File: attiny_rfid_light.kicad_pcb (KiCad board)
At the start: 2 copper layers, 76 x 99.1 mm, 27 parts, among them IC1 EM4095, U1 ESP32-WROOM-32, U2 NCP1117-3.3_SOT223

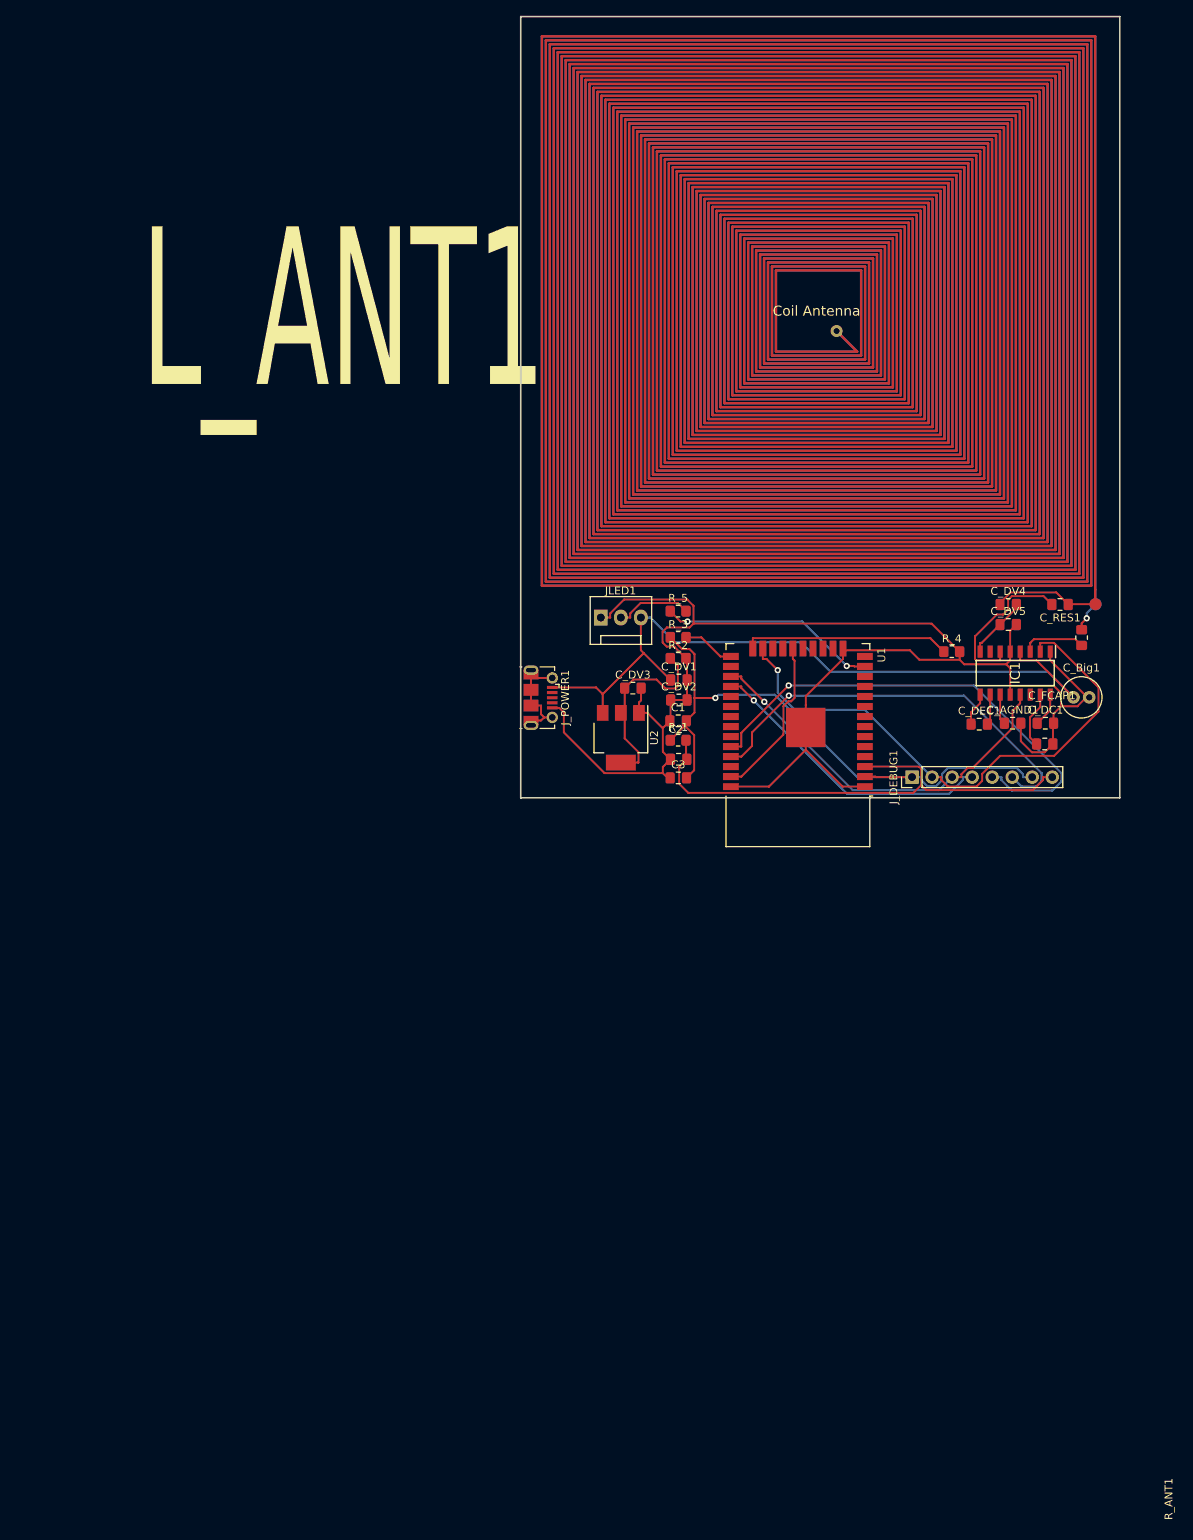
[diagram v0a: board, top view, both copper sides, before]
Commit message: Update fix antenna direction and missing shd trace
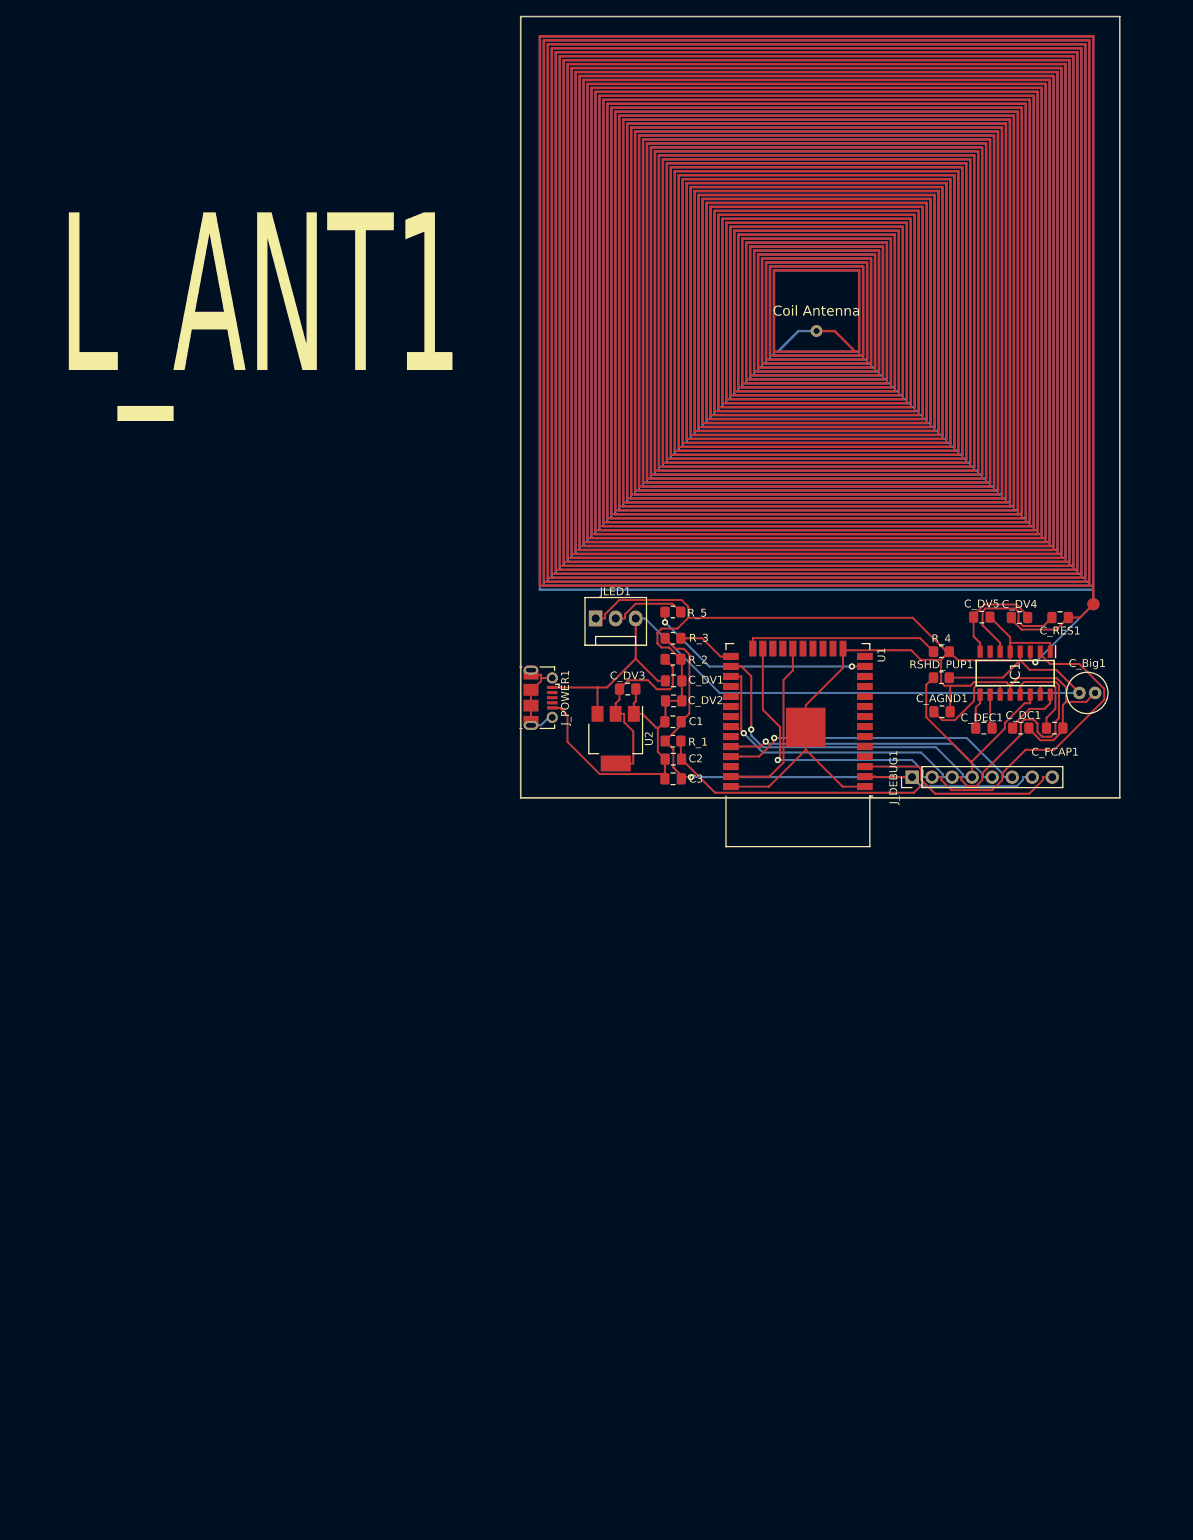
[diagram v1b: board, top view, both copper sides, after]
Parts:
- removed R_ANT1: 10, Resistor_SMD:R_0805_2012Metric_Pad1.20x1.40mm_HandSolder
- added RSHD_PUP1: 10K, Resistor_SMD:R_0805_2012Metric_Pad1.20x1.40mm_HandSolder, F.Cu at (119.4, 139.7)
- C_AGND1, C_DEC1: value C -> 100nf
- C_DC1: value C -> 10NF
- C_DV4: value C -> 0.1nf
- C_DV5: value C -> 3.7nf
- C_FCAP1: value C -> 10nf
- C_RES1: value C -> 2.2nf
- L_ANT1: footprint pcb_inductors:60_turn_square_inductor -> pcb_inductors:60_turn_square_inductor_corrected
- moved C_AGND1 9.07 mm to (119.5, 144.0)
- moved C_DV5 3.47 mm to (124.5, 132.0)
- moved C_DC1 3.18 mm to (129.4, 146.1)
- moved C_FCAP1 2.38 mm to (133.7, 146.1)
- moved C_DV4 2.19 mm to (129.3, 132.1)
- moved C_RES1 1.65 mm to (134.4, 132.1)
- moved R_4 1.32 mm to (119.4, 136.4)
- moved C_Big1 0.94 mm to (136.9, 141.6)
- moved C_DEC1 0.78 mm to (124.8, 146.1)
- moved C2 0.67 mm to (85.4, 150.0)
- moved C1 0.67 mm to (85.3, 145.3)
- moved C_DV1 0.67 mm to (85.4, 140.1)
- moved C_DV2 0.67 mm to (85.4, 142.6)
- moved R_3 0.67 mm to (85.4, 134.7)
- moved R_5 0.67 mm to (85.3, 131.4)
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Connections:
- IC1 pad 14: unconnected-(IC1-Pad14) -> Net-(IC1-Pad14)
- J_DEBUG1 pad 4: Net-(J_DEBUG1-Pad4) -> Net-(IC1-Pad14)
- L_ANT1 pad 2: Net-(L_ANT1-Pad2) -> Net-(IC1-Pad3)
- U1 pad 26: unconnected-(U1-Pad26) -> Net-(IC1-Pad14)
- U1 pad 28: Net-(J_DEBUG1-Pad4) -> unconnected-(U1-Pad28)
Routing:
- net Net-(IC1-Pad14): track 0.00 -> 68.5 mm, vias 0 -> 1
- net Net-(J_DEBUG1-Pad4): track 37.4 -> 0.00 mm, vias 1 -> 0
- net Net-(J_DEBUG1-Pad5): track 62.0 -> 35.5 mm
- net Net-(IC1-Pad13): track 50.0 -> 70.6 mm
- net Net-(J_DEBUG1-Pad6): track 53.2 -> 39.2 mm
- net +5V: track 94.8 -> 105.9 mm
- net GND: track 205.9 -> 215.1 mm
- net Net-(C_AGND1-Pad1): track 3.85 -> 12.7 mm
- net +3V3: track 79.8 -> 73.5 mm
- net Net-(C_DV4-Pad2): track 7.98 -> 13.2 mm
- net Net-(IC1-Pad2): track 70.8 -> 75.7 mm
- net Net-(IC1-Pad3): track 8.15 -> 12.3 mm, vias 0 -> 1
- net Net-(L_ANT1-Pad2): track 3.96 -> 0.00 mm, vias 1 -> 0
- net Net-(C_RES1-Pad2): track 20.3 -> 17.1 mm
- net Net-(C_DC1-Pad1): track 4.32 -> 7.36 mm
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
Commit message: v3
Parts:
- removed C3: 1uf, Capacitor_SMD:C_0805_2012Metric_Pad1.18x1.45mm_HandSolder
- removed R_5: 490, Resistor_SMD:R_0805_2012Metric_Pad1.20x1.40mm_HandSolder
- added C_RESOptional1: NA, Capacitor_SMD:C_0805_2012Metric_Pad1.18x1.45mm_HandSolder, F.Cu at (131.9, 130.6)
- added m2: MountingHole_2.1mm, MountingHole:MountingHole_2.1mm, F.Cu at (114.3, 132.1)
- added m2: MountingHole_2.1mm, MountingHole:MountingHole_2.1mm, F.Cu at (68.6, 132.1)
- added m2: MountingHole_2.1mm, MountingHole:MountingHole_2.1mm, F.Cu at (138.4, 152.6)
- added m2: MountingHole_2.1mm, MountingHole:MountingHole_2.1mm, F.Cu at (68.4, 152.4)
- C1: value 100uf -> 0.1uf
- C2: value 0.1uf -> 1uf
- C_Big1: value 10uf -> 100uf
- C_DV3: value 22uf -> 0.1nf
- C_DV4: value 0.1nf -> 3.7nf split between 2
- C_DV5: value 3.7nf -> 3.7nf split between 2
- R_2: value 3.3k -> 5k1 or 5k? was 5k og
- R_3: value 5k -> 490
- R_4: value 5k -> 5k1 og was 5k
- moved C1 51.4 mm to (136.6, 149.2), turned to 180 degrees
- moved C_DV3 42.6 mm to (121.5, 133.1)
- moved C_DV1 40.4 mm to (125.4, 146.3)
- moved C2 32.6 mm to (115.8, 138.5)
- moved R_4 32.0 mm to (87.4, 137.2)
- moved R_1 30.8 mm to (115.8, 143.3), turned to 180 degrees
- moved C_AGND1 11.9 mm to (131.1, 146.3)
- moved C_DV2 10.1 mm to (87.5, 152.5)
- moved RSHD_PUP1 8.53 mm to (116.0, 147.5)
- moved C_DC1 7.19 mm to (136.6, 145.8)
- moved C_DEC1 5.18 mm to (121.0, 142.6), turned to 90 degrees
- moved C_FCAP1 4.82 mm to (136.6, 142.2)
- moved C_Big1 4.48 mm to (136.9, 137.2)
- moved C_DV4 3.32 mm to (126.4, 130.5)
- moved R_2 3.17 mm to (87.5, 139.7)
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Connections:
- C1 pad 2: +3V3 -> Net-(C1-Pad2)
- C2 pad 2: Net-(C2-Pad2) -> +3V3
- C_DV2 pad 1: GND -> +3V3
- C_DV3 pad 2: GND -> Net-(C_DV3-Pad2)
- C_DV4 pad 1: Net-(C_DV4-Pad1) -> Net-(C_DV3-Pad2)
- C_DV4 pad 2: Net-(C_DV4-Pad2) -> GND
- C_DV5 pad 1: Net-(C_DV4-Pad2) -> Net-(C_DV3-Pad2)
- C_RES1 pad 1: Net-(C_DV4-Pad1) -> Net-(C_DV3-Pad1)
- IC1 pad 7: unconnected-(IC1-Pad7) -> +5V
- IC1 pad 8: Net-(C_DV4-Pad2) -> Net-(C_DV3-Pad2)
- J_DEBUG1 pad 1: +3V3 -> GND
- J_DEBUG1 pad 2: Net-(IC1-Pad2) -> +3V3
- J_DEBUG1 pad 3: Net-(IC1-Pad13) -> +5V
- J_DEBUG1 pad 4: Net-(IC1-Pad14) -> Net-(J_DEBUG1-Pad4)
- J_DEBUG1 pad 7: +3V3 -> Net-(J_DEBUG1-Pad7)
- J_DEBUG1 pad 8: Net-(C2-Pad2) -> Net-(C1-Pad2)
- L_ANT1 pad 1: Net-(C_DV4-Pad1) -> Net-(C_DV3-Pad1)
- R_1 pad 2: Net-(C2-Pad2) -> Net-(C1-Pad2)
- R_2 pad 1: Net-(C_DV3-Pad1) -> +3V3
- R_2 pad 2: GND -> Net-(J_DEBUG1-Pad7)
- R_3 pad 1: +3V3 -> Net-(JLED1-Pad2)
- U1 pad 13: Net-(R_5-Pad1) -> Net-(R_3-Pad2)
- U1 pad 25: Net-(R_3-Pad2) -> Net-(J_DEBUG1-Pad7)
- U1 pad 29: unconnected-(U1-Pad29) -> Net-(J_DEBUG1-Pad4)
- U1 pad 3: Net-(C2-Pad2) -> Net-(C1-Pad2)
- U2 pad 2: Net-(C_DV3-Pad1) -> +3V3
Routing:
- net Net-(C2-Pad2): track 62.4 -> 0.00 mm
- net Net-(J_DEBUG1-Pad7): track 0.00 -> 50.1 mm, vias 0 -> 1
- net Net-(J_DEBUG1-Pad4): track 0.00 -> 37.8 mm, vias 0 -> 1
- net Net-(IC1-Pad2): track 75.7 -> 38.3 mm, vias 1 -> 2
- net Net-(C1-Pad2): track 0.00 -> 37.2 mm, vias 0 -> 1
- net +5V: track 105.9 -> 138.3 mm
- net Net-(IC1-Pad13): track 70.6 -> 38.9 mm, vias 1 -> 2
- net Net-(R_5-Pad1): track 29.0 -> 0.00 mm, vias 2 -> 0
- net Net-(IC1-Pad14): track 68.5 -> 45.5 mm, vias 1 -> 3
- net Net-(R_3-Pad2): track 7.29 -> 28.1 mm
- net GND: track 215.1 -> 200.5 mm, vias 0 -> 22
- net Net-(R_4-Pad1): track 24.9 -> 11.4 mm
- net Net-(C_DV4-Pad2): track 13.2 -> 0.00 mm
- net Net-(C_DV4-Pad1): track 12.5 -> 0.00 mm
- net +3V3: track 73.5 -> 85.3 mm
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- added copper zone on B.Cu, net GND
- added copper zone on F.Cu, net GND
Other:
- board size 76 x 99.1 mm -> 75 x 99.1 mm
